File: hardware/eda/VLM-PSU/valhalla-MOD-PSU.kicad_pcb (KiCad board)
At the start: 2 copper layers, 99.6 x 99.6 mm, 58 parts, among them J1 MAINS, J2 DC, J3 BUS, J4 GPIO, J5 POWER, Q1 BTA08-600CW, Q10 IRF9Z34N, Q2 2N3904, Q3 2N3906, Q4 2N3906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

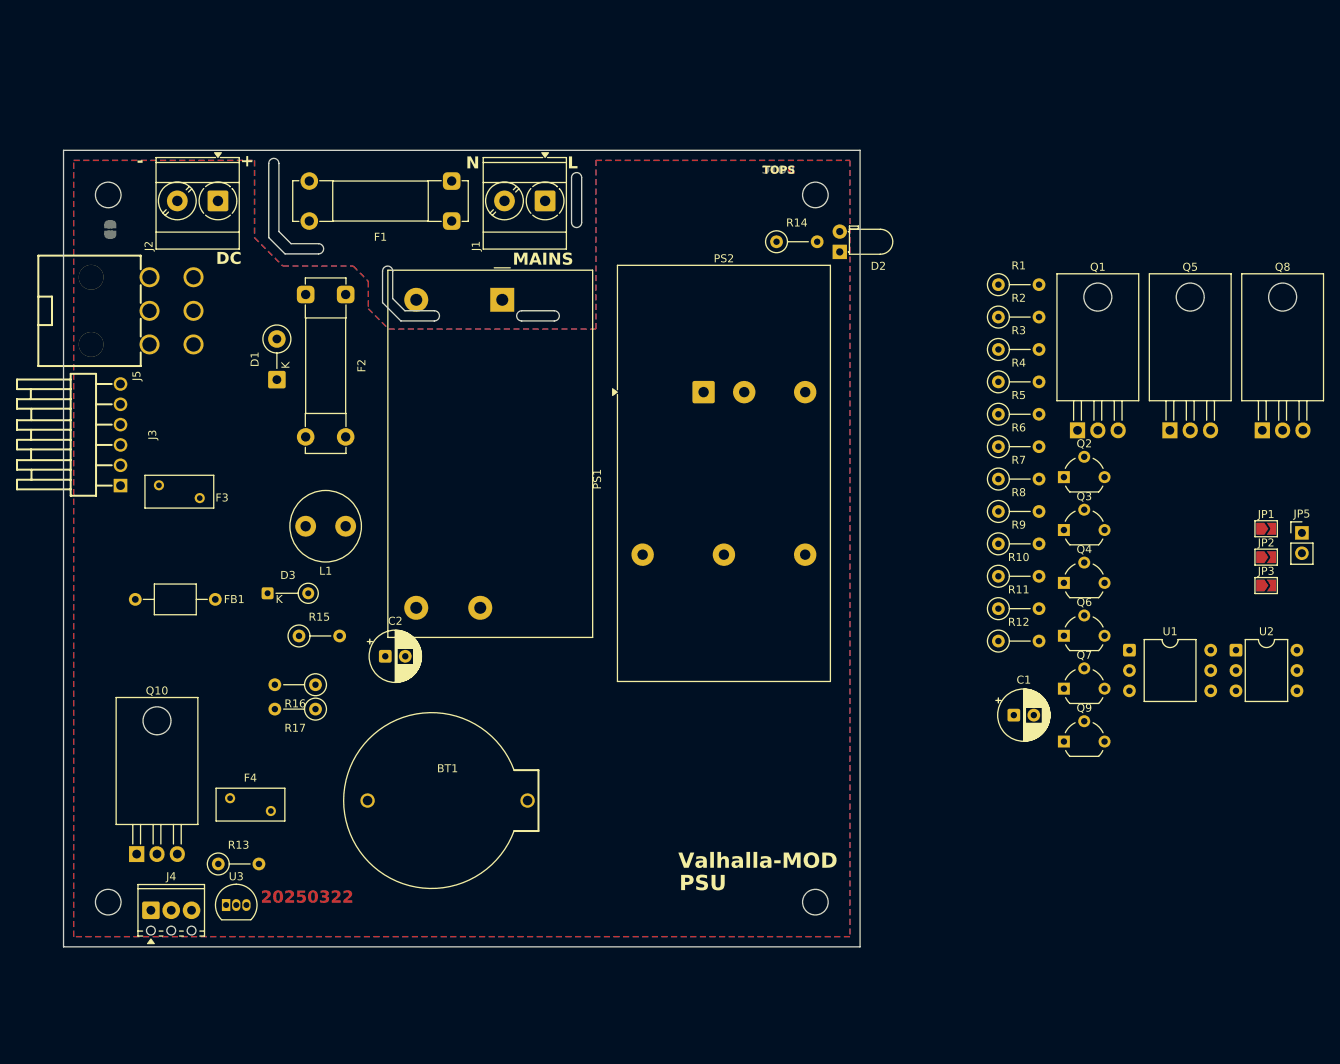
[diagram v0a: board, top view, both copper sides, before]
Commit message: UPDATE: tentative component placement for MOD-PSU
  - everything fits with room to spare
  - clearance/creepage for the mains section appears fine
  - zones/slots are next.
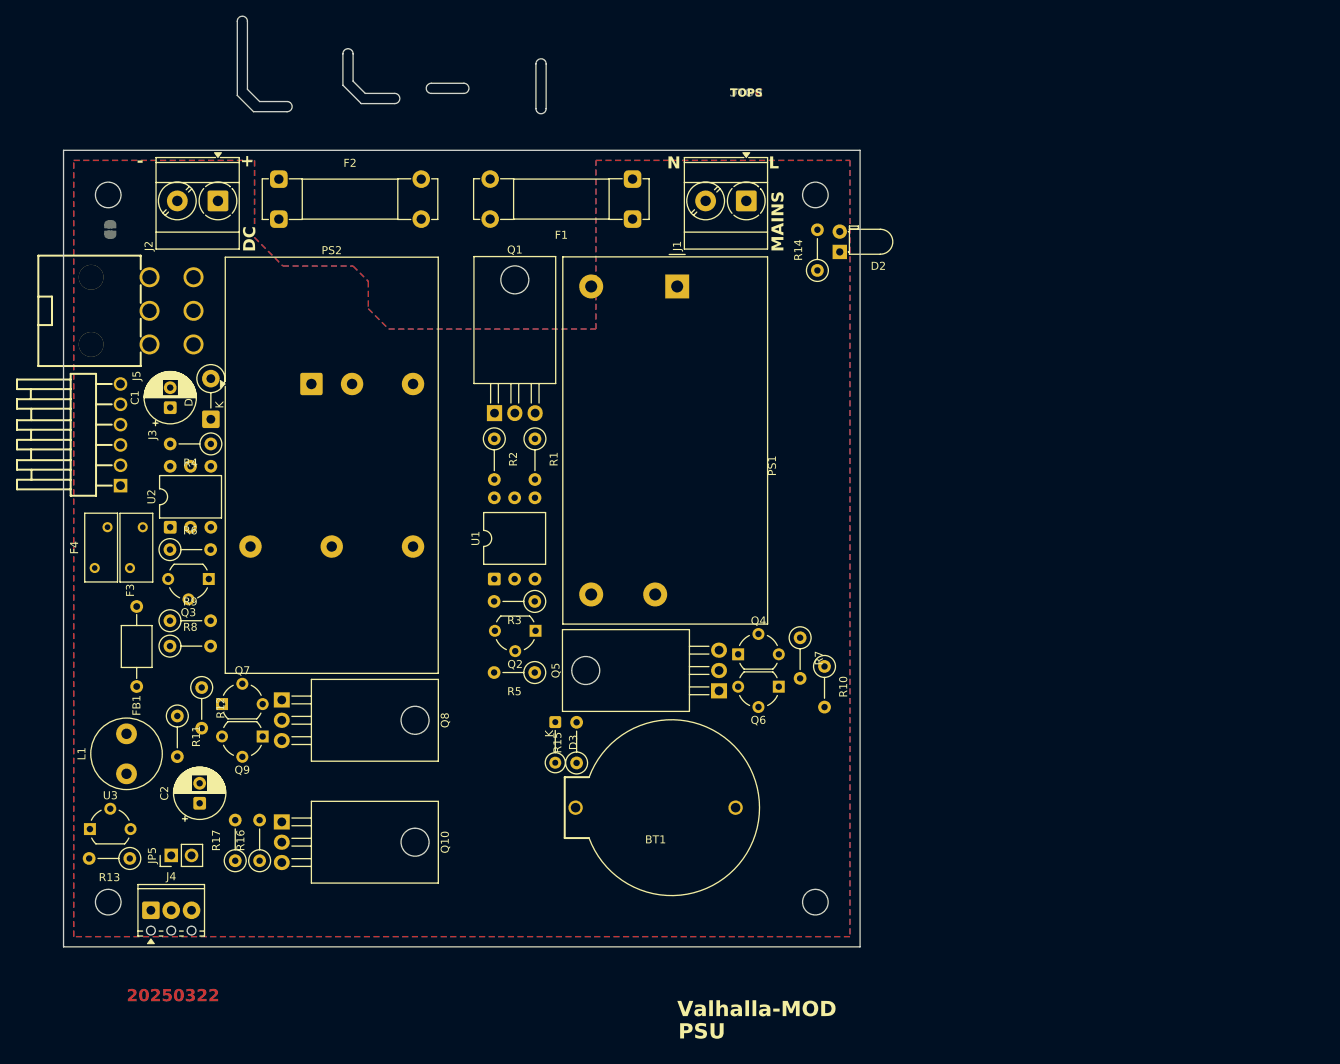
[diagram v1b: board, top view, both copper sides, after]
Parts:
- removed JP1: ~{REMOTE}, Jumper:SolderJumper-2_P1.3mm_Open_TrianglePad1.0x1.5mm
- removed JP2, JP3: SINGLE, Jumper:SolderJumper-2_P1.3mm_Open_TrianglePad1.0x1.5mm
- U3: footprint Package_TO_SOT_THT:TO-92_Inline -> Package_TO_SOT_THT:TO-92_Wide
- moved JP5 147.0 mm to (38.9, 113.5), turned to 90 degrees
- moved U2 134.1 mm to (38.7, 72.5), turned to 90 degrees
- moved Q8 127.1 mm to (52.7, 94.1), turned to -90 degrees
- moved C1 112.2 mm to (38.7, 57.6), turned to 90 degrees
- moved Q3 107.1 mm to (43.6, 79.0), turned to 180 degrees
- moved Q7 105.3 mm to (45.2, 94.6)
- moved R8 104.9 mm to (38.7, 87.4)
- moved R6 104.3 mm to (38.7, 75.3)
- moved R9 104.0 mm to (38.7, 84.2)
- moved R11 103.5 mm to (39.6, 96.1), turned to -90 degrees
- moved Q9 100.2 mm to (50.3, 98.7), turned to 180 degrees
- moved R12 99.8 mm to (42.7, 92.6), turned to -90 degrees
- moved R4 98.7 mm to (43.8, 62.1), turned to 180 degrees
- moved U1 79.9 mm to (79.2, 79.0), turned to 90 degrees
- moved Q1 72.9 mm to (79.3, 58.3)
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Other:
- board size 99.6 x 99.6 mm -> 99.6 x 116.3 mm

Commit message: UPDATE: progress on MOD-PSU layout
  - zones and slots done
  - heatsink pours and stiches done
  - routing is next.
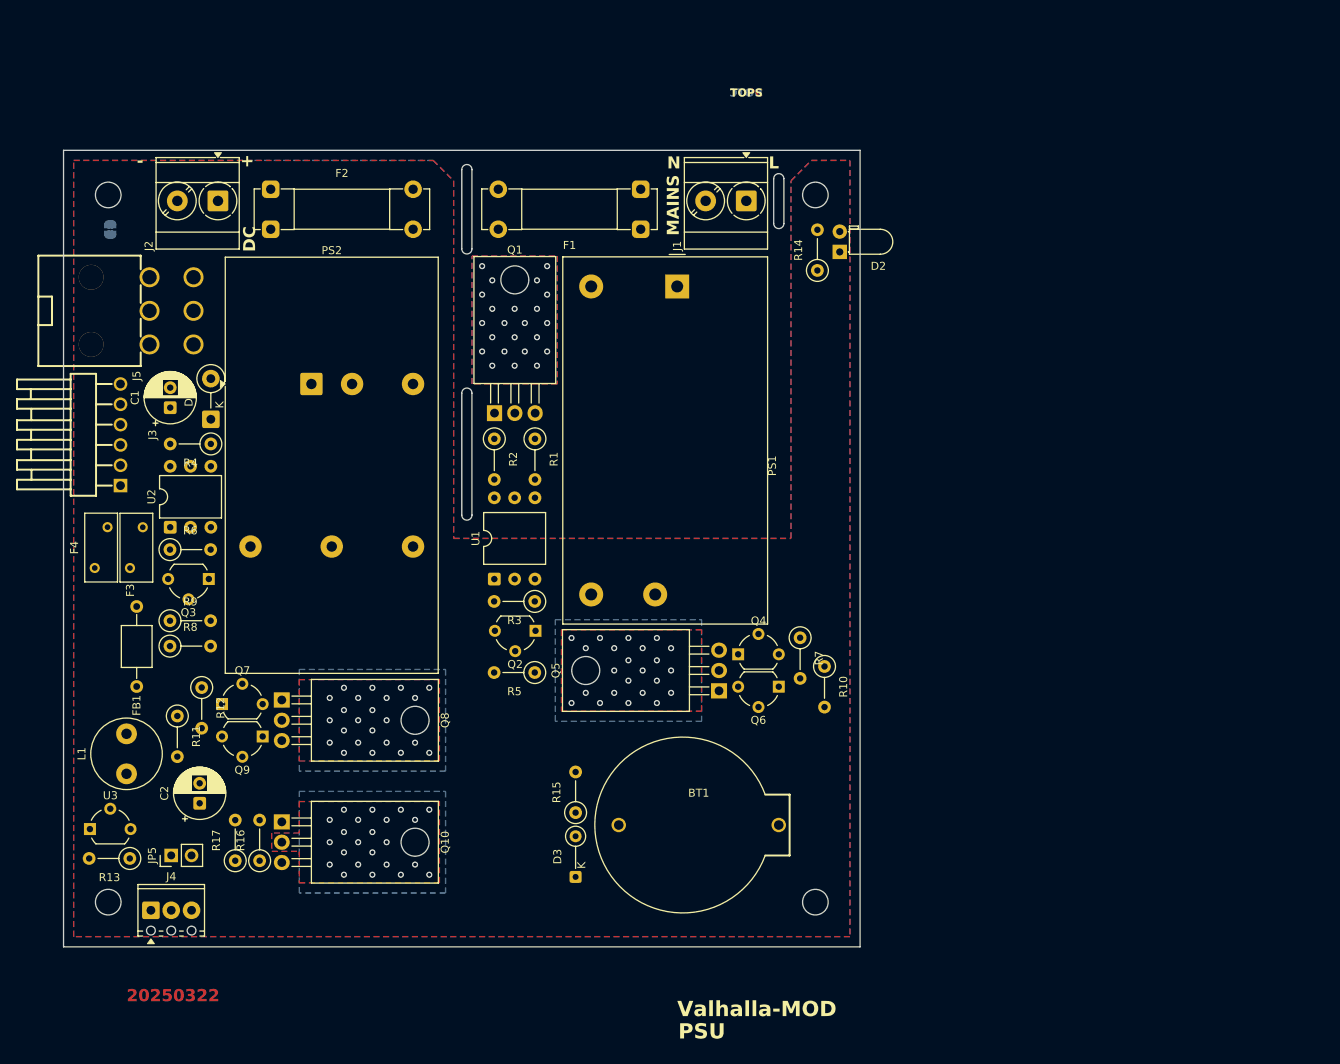
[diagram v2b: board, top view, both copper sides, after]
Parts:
- moved D3 19.5 mm to (89.4, 116.2), turned to 90 degrees
- moved R15 6.21 mm to (89.4, 108.2)
- moved BT1 5.81 mm to (104.8, 109.7), turned to 0 degrees
- moved F1 1.63 mm to (97.5, 35.3)
- moved F2 1.62 mm to (51.3, 30.3)
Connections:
- net Net-(Q10-D) renamed /RAW_LVCC
- C2 pad 1: Net-(Q10-S) -> /RAW_VCC
- FB1 pad 1: Net-(Q10-S) -> /RAW_VCC
- L1 pad 1: Net-(Q10-S) -> /RAW_VCC
- Q10 pad 3: Net-(Q10-S) -> /RAW_VCC
- Q5 pad 2: Net-(Q10-S) -> Net-(PS1-+Vo)
- Q5 pad 3: Net-(PS1-+Vo) -> /RAW_VCC
- Q6 pad 1: Net-(Q10-S) -> /RAW_VCC
- Q8 pad 3: Net-(Q10-S) -> /RAW_VCC
- Q9 pad 1: Net-(Q10-S) -> /RAW_VCC
- R13 pad 1: Net-(Q10-S) -> /RAW_VCC
- R14 pad 1: Net-(Q10-S) -> /RAW_VCC
- R16 pad 1: Net-(Q10-S) -> /RAW_VCC
- U3 pad 2: Net-(Q10-S) -> /RAW_VCC
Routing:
- net _Q1_HEATSINK: vias 0 -> 23
- net /RAW_VCC: vias 0 -> 46
- net /RAW_LVCC: vias 0 -> 23
- added copper zone on B.Cu, net /RAW_LVCC
- added copper zone on F.Cu, net /RAW_LVCC
- added copper zone on B.Cu, net /RAW_VCC
- added copper zone on F.Cu, net /RAW_VCC
- added copper zone on B.Cu, net _Q1_HEATSINK
- added copper zone on F.Cu, net _Q1_HEATSINK
- removed copper zone on F.Cu, net Net-(Q10-S)
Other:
- board size 99.6 x 116.3 mm -> 99.6 x 99.6 mm

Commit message: UPDATE: progress on MOD-PSU
  - routing done, including copper heatsinks
  - silkscreen is last.
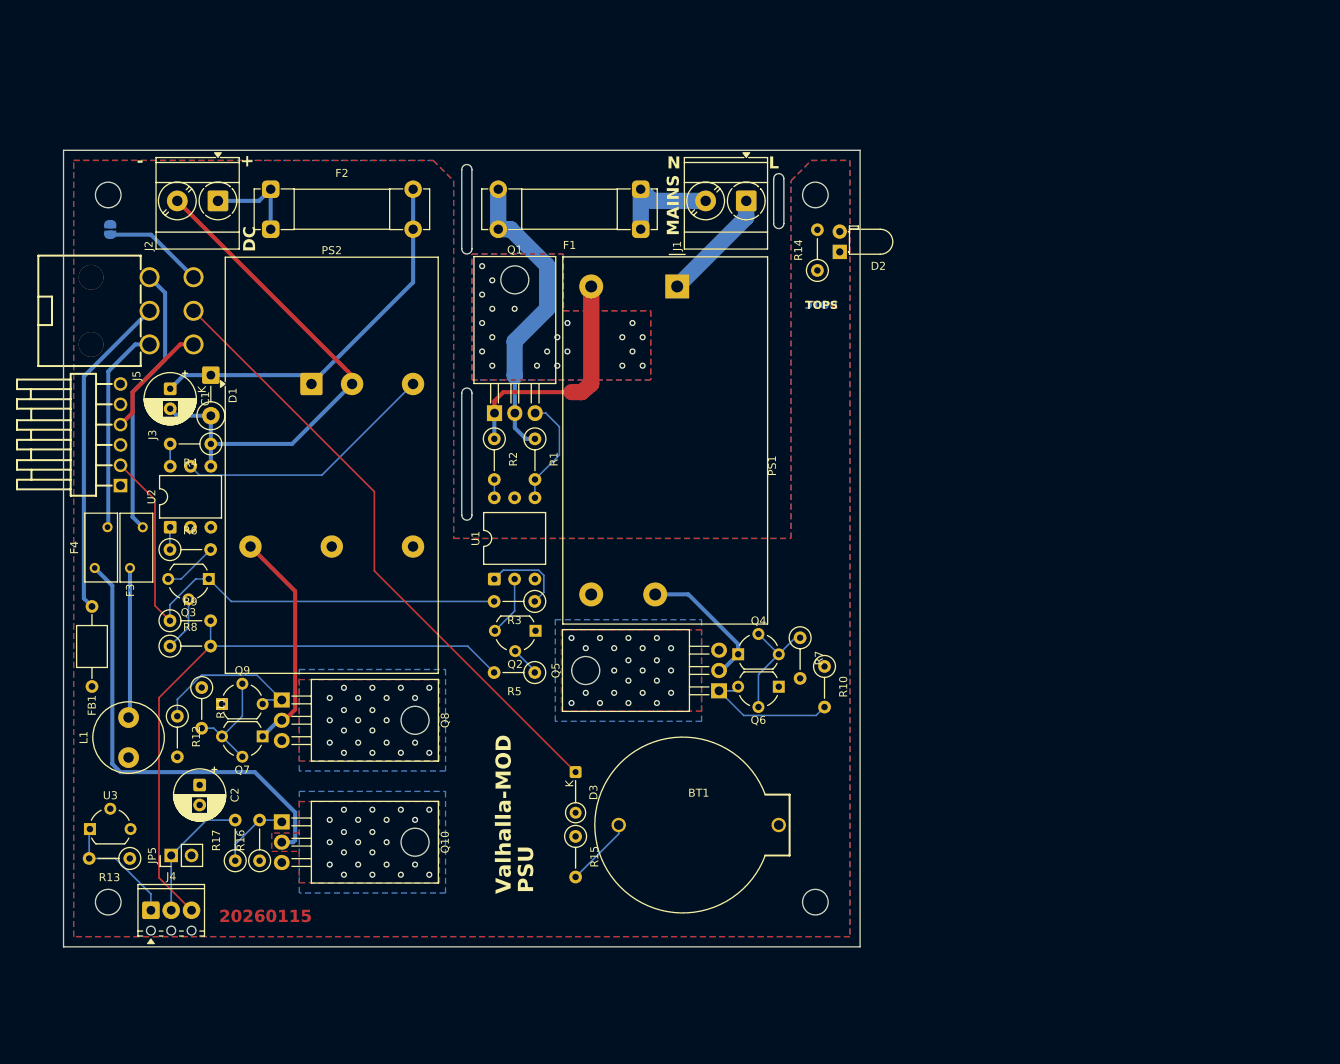
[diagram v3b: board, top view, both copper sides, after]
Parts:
- moved D3 13.1 mm to (89.4, 103.1), turned to -90 degrees
- moved Q9 6.50 mm to (45.2, 94.6), turned to 0 degrees
- moved Q7 6.49 mm to (50.3, 98.7), turned to 180 degrees
- moved FB1 5.59 mm to (29.0, 92.4)
- moved D1 5.52 mm to (43.8, 53.5), turned to -90 degrees
- moved R12 4.71 mm to (39.6, 96.1)
- moved R11 4.68 mm to (42.7, 92.6)
- moved R15 2.97 mm to (89.4, 111.2), turned to -90 degrees
- moved C1 2.36 mm to (38.7, 55.2), turned to -90 degrees
- moved C2 2.29 mm to (42.4, 104.7), turned to -90 degrees
- moved L1 2.05 mm to (33.5, 101.3)
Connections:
- Q7 pad 3: Net-(Q7-C) -> Net-(Q7-B)
- Q8 pad 1: Net-(Q7-C) -> Net-(Q8-G)
- Q9 pad 3: Net-(Q7-B) -> Net-(Q8-G)
- R11 pad 2: Net-(Q7-C) -> Net-(Q7-B)
- R12 pad 1: Net-(Q7-B) -> Net-(Q8-G)
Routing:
- net /BVCC: track 0.00 -> 77.4 mm
- net /PS_ON/~{OFF}: track 0.00 -> 77.4 mm
- net /BUS_DVCC: track 0.00 -> 67.0 mm
- net Net-(D1-A): track 0.00 -> 64.4 mm
- net /RAW_LVCC: track 0.00 -> 56.0 mm
- net Net-(D1-K): track 0.00 -> 48.4 mm
- net /DVCC: track 0.00 -> 40.8 mm
- net Net-(Q1-A2): track 0.00 -> 38.0 mm
- net /AVCC: track 0.00 -> 34.3 mm
- net Net-(PS2-Control): track 0.00 -> 33.0 mm
- net Net-(PS1-AC/L): track 0.00 -> 29.9 mm
- net Net-(PS2-+OUT): track 0.00 -> 28.1 mm
- net /LVCC: track 0.00 -> 26.1 mm
- net Net-(Q8-G): track 0.00 -> 21.0 mm
- net Net-(F3-Pad1): track 0.00 -> 18.8 mm
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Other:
- board text added: "20260115"
- board text removed: "20250322"

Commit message: DONE: MOD-PSU silkscreen complete, DRC pass, RTM
 - also backfilled constraints files for both MOD-PSU and MOD-XVR(4IO)
 - mechanical extraction and specification update is next, then update
   of the template, then on to MOD-CPU(ATMega).
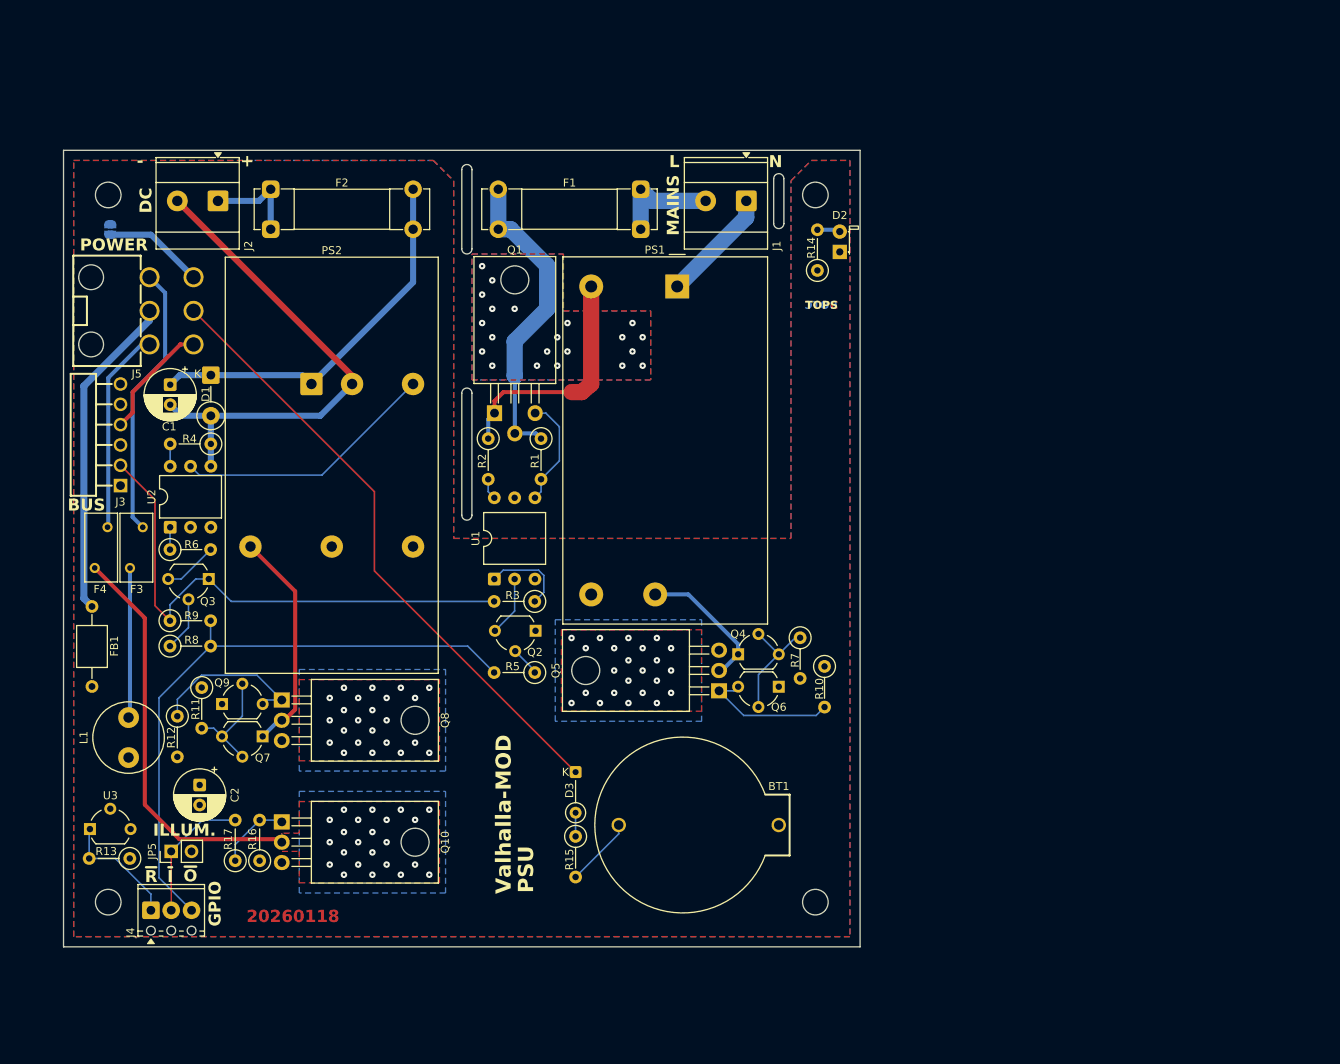
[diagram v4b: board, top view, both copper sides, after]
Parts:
- moved R1 0.76 mm to (85.1, 61.4)
- moved R2 0.76 mm to (78.5, 61.4)
- moved JP5 0.51 mm to (38.9, 113.0)
- moved C1 0.51 mm to (38.7, 54.7)
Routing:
- net /RAW_LVCC: track 56.0 -> 51.2 mm
- net Net-(D3-A): track 0.00 -> 2.95 mm
- net Net-(D2-A): track 0.00 -> 2.89 mm
- net Net-(D1-A): track 64.4 -> 63.2 mm
- net Net-(Q1-A2): track 38.0 -> 39.2 mm
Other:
- board text added: "20260118"
- board text added: "BUS"
- board text added: "GPIO"
- board text added: "ILLUM."
- board text added: "K"
- board text added: "POWER"
- board text added: "~{I}"
- board text added: "~{O}"
- board text added: "~{R}"
- board text removed: "20260115"

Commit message: BUGFIX: main power connector pinout is not the same as the normal one
  - main power connector is sized for more current, has a different
    size and a different layout (2-row vs. 1-row). Thus, there is a
    numerically different way of keeping sensitive lines apart
  - this became apparent in MOD-PSU which uses both.
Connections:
- J3 pad 1: unconnected-(J3-Pin_1-Pad1) -> /BUS_DVCC
- J3 pad 2: /BUS_DVCC -> /DGND
- J3 pad 4: /DGND -> unconnected-(J3-Pin_4-Pad4)
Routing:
- net /DGND: track 14.8 -> 19.9 mm
- net /BUS_DVCC: track 67.0 -> 64.5 mm
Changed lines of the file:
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@@
 	(net 17 "Net-(D2-A)")
 	(net 18 "Net-(Q1-G)")
-	(net 19 "unconnected-(J3-Pin_1-Pad1)")
+	(net 19 "unconnected-(J3-Pin_4-Pad4)")
 	(net 20 "unconnected-(J3-Pin_5-Pad5)")
 	(net 21 "/BUS_DVCC")
@@
 			(layers "*.Cu" "*.Mask")
 			(remove_unused_layers no)
-			(net 19 "unconnected-(J3-Pin_1-Pad1)")
+			(net 21 "/BUS_DVCC")
 			(pinfunction "Pin_1")
-			(pintype "passive+no_connect")
+			(pintype "passive")
 		)
 		(pad "2" thru_hole circle
@@
 			(layers "*.Cu" "*.Mask")
 			(remove_unused_layers no)
-			(net 21 "/BUS_DVCC")
+			(net 1 "/DGND")
 			(pinfunction "Pin_2")
 			(pintype "passive")
@@
 			(layers "*.Cu" "*.Mask")
 			(remove_unused_layers no)
-			(net 1 "/DGND")
+			(net 19 "unconnected-(J3-Pin_4-Pad4)")
 			(pinfunction "Pin_4")
-			(pintype "passive")
+			(pintype "passive+no_connect")
 		)
 		(pad "5" thru_hole circle
@@
 	)
 	(segment
-		(start 34.036 55.626)
-		(end 39.996 49.666)
+		(start 39.996 49.666)
+		(end 41.6495 49.666)
 		(width 0.508)
 		(layer "F.Cu")
@@
 	)
 	(segment
-		(start 39.996 49.666)
-		(end 41.6495 49.666)
+		(start 34.036 63.2575)
+		(end 34.036 55.626)
 		(width 0.508)
 		(layer "F.Cu")
@@
 	)
 	(segment
-		(start 34.036 58.1775)
-		(end 34.036 55.626)
+		(start 34.036 55.626)
+		(end 39.996 49.666)
 		(width 0.508)
 		(layer "F.Cu")
@@
 	)
 	(segment
-		(start 32.5235 59.69)
-		(end 34.036 58.1775)
+		(start 32.5235 64.77)
+		(end 34.036 63.2575)
 		(width 0.508)
 		(layer "F.Cu")
@@
 	)
 	(segment
-		(start 36.83 69.0765)
+		(start 36.83 71.628)
 		(end 36.83 82.325)
 		(width 0.2032)
@@
 	)
 	(segment
-		(start 32.5235 64.77)
-		(end 36.83 69.0765)
+		(start 32.5235 67.31)
+		(end 32.5235 67.3215)
+		(width 0.2032)
+		(layer "F.Cu")
+		(net 21)
+	)
+	(segment
+		(start 32.5235 67.3215)
+		(end 36.83 71.628)
 		(width 0.2032)
 		(layer "F.Cu")
@@
 			(radius 0.254)
 			(island_removal_mode 1)
-			(island_area_min 9.999998)
+			(island_area_min 9.999997)
 		)
 		(polygon
@@
 			(radius 0.254)
 			(island_removal_mode 1)
-			(island_area_min 9.999998)
+			(island_area_min 9.999997)
 		)
 		(polygon
